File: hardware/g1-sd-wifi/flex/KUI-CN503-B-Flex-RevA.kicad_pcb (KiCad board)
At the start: 2 copper layers, 10.7 x 59.9 mm, 2 parts, among them J1 CN503 row B solder contacts, J2 20-pin bottom-contact FPC tail

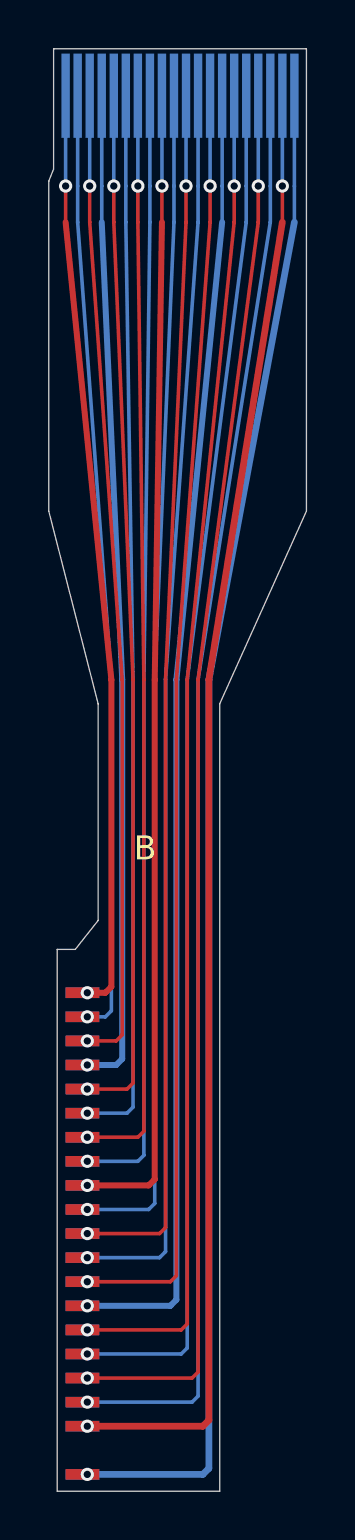
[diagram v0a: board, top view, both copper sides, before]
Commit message: G1 safety: fuse the host 3.3-V entry; no console 5 V on the flex or carrier
Host 3.3 V reached about 30 carrier parts straight from two flex contacts,
and the two console-5-V contacts were joined by an unused carrier trace;
a short on either would load a console supply through 0.5 A connector
contacts with no fuse anywhere. Now:

- F21 (0467.500NR, 0.5 A fast, same 467 family as F20) sits between the one
  remaining 3.3-V entry, J51 B1, and CONSOLE_3V3. If it opens the buffers
  lose VCCB and isolate, and U25 reports the host rail absent.
- CN503 A1 (second 3.3 V) and A3/B3 (5 V) get no flex copper at all: no
  landing pad, no trace, only an unconnected mating finger, so a chafed
  flex cannot short a console supply. Their carrier socket pins are bare.
  flex-interface.json lists them; the flex and carrier generators and both
  checks read that list. Flex ERC/DRC/parity 0; carrier ERC 0, integration
  check pass (362 parts).
- The DSN export keeps the 5-V and storage supply nets on the 1 oz outer
  layers: on 0.5 oz inner copper a 0.25 mm track at the fuse current would
  overheat (IPC-2221).
- F21 is placed by the floorplan next to J51; board DRC 0, parity 0
  (unrouted).

Co-Authored-By: Claude Opus 5.5 <noreply@anthropic.com>
Claude-Session: https://claude.ai/code/session_01Gp9EYc2r9fMpZ7V8WtfonZ
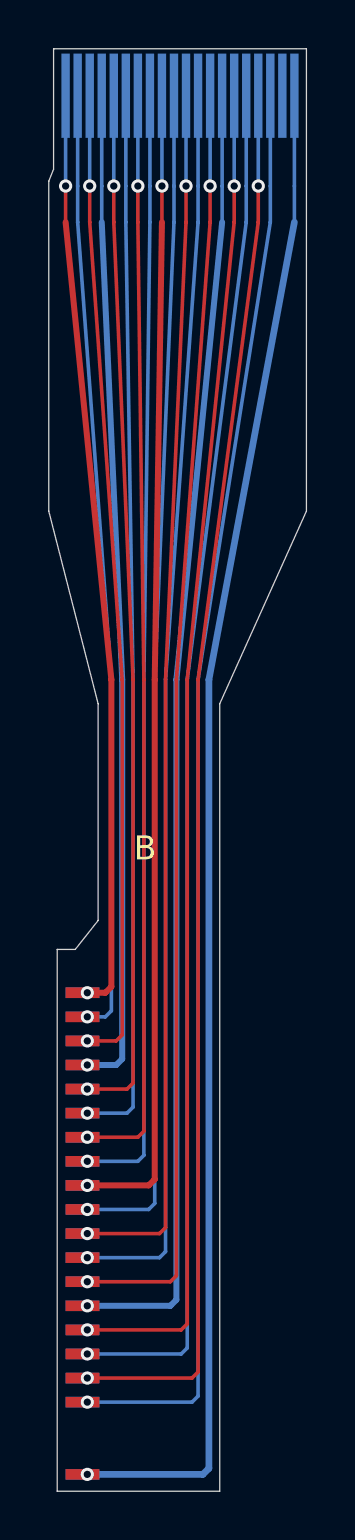
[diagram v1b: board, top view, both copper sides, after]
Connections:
- J2 pad 19: /CN503_B3_CONSOLE_5V -> unconnected-(J2-Pad19)
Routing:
- net /CN503_B3_CONSOLE_5V: track 60.8 -> 0.00 mm, vias 2 -> 0
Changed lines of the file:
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@@
 (net 0 "")
 (net 1 "/CN503_B1_CONSOLE_3V3")
-(net 2 "/CN503_B3_CONSOLE_5V")
 (net 3 "/CN503_B4_ATA_DD6")
 (net 4 "/CN503_B5_ATA_DD9")
@@
 (net 19 "/CN503_B20_ATA_CS1n")
 (net 20 "/CN503_B21_GND")
+(net 21 "unconnected-(J2-Pad19)")
 (footprint "KUI_Flex:CN503_B_20_SolderLanding_1.00mm" (layer "F.Cu") (at 100.0 100.0) (attr board_only exclude_from_pos_files exclude_from_bom)
 (property "Reference" "J1" (at 0 0) (layer "F.Fab") (effects (font (size .8 .8)) hide))
@@
 (pad "1" smd rect (at 0.7 0) (size 1.4 .44) (layers "F.Cu" "F.Mask") (net 1 "/CN503_B1_CONSOLE_3V3") (solder_mask_margin .29))
 (pad "1" smd rect (at 0.7 0) (size 1.4 .44) (layers "B.Cu" "B.Mask") (net 1 "/CN503_B1_CONSOLE_3V3") (solder_mask_margin .29))
-(pad "3" smd rect (at 0.7 -2) (size 1.4 .44) (layers "F.Cu" "F.Mask") (net 2 "/CN503_B3_CONSOLE_5V") (solder_mask_margin .29))
-(pad "3" smd rect (at 0.7 -2) (size 1.4 .44) (layers "B.Cu" "B.Mask") (net 2 "/CN503_B3_CONSOLE_5V") (solder_mask_margin .29))
 (pad "4" smd rect (at 0.7 -3) (size 1.4 .44) (layers "F.Cu" "F.Mask") (net 3 "/CN503_B4_ATA_DD6") (solder_mask_margin .29))
 (pad "4" smd rect (at 0.7 -3) (size 1.4 .44) (layers "B.Cu" "B.Mask") (net 3 "/CN503_B4_ATA_DD6") (solder_mask_margin .29))
@@
 (property "Value" "20-pin bottom-contact FPC tail" (at 0 0) (layer "F.Fab") (effects (font (size .8 .8)) hide))
 (pad "20" smd rect (at 9.5 -57.25) (size .35 3.5) (layers "B.Cu" "B.Mask") (net 1 "/CN503_B1_CONSOLE_3V3") (solder_mask_margin .10))
-(pad "19" smd rect (at 9 -57.25) (size .35 3.5) (layers "B.Cu" "B.Mask") (net 2 "/CN503_B3_CONSOLE_5V") (solder_mask_margin .10))
+(pad "19" smd rect (at 9 -57.25) (size .35 3.5) (layers "B.Cu" "B.Mask") (net 21 "unconnected-(J2-Pad19)") (solder_mask_margin .10))
 (pad "18" smd rect (at 8.5 -57.25) (size .35 3.5) (layers "B.Cu" "B.Mask") (net 3 "/CN503_B4_ATA_DD6") (solder_mask_margin .10))
 (pad "17" smd rect (at 8 -57.25) (size .35 3.5) (layers "B.Cu" "B.Mask") (net 4 "/CN503_B5_ATA_DD9") (solder_mask_margin .10))
@@
 (segment (start 109.5 48) (end 109.5 46.5) (width 0.15) (layer "B.Cu") (net 1))
 (segment (start 109.5 46.5) (end 109.5 42.75) (width 0.15) (layer "B.Cu") (net 1))
-(segment (start 100.7 98) (end 100.9 98) (width 0.15) (layer "F.Cu") (net 2))
-(segment (start 100.7 98) (end 100.9 98) (width 0.15) (layer "B.Cu") (net 2))
-(segment (start 100.9 98) (end 105.7 98) (width 0.28) (layer "F.Cu") (net 2))
-(segment (start 105.7 98) (end 105.95 97.75) (width 0.28) (layer "F.Cu") (net 2))
-(segment (start 105.95 97.75) (end 105.95 67) (width 0.28) (layer "F.Cu") (net 2))
-(segment (start 105.95 67) (end 109 48) (width 0.28) (layer "F.Cu") (net 2))
-(segment (start 109 48) (end 109 46.5) (width 0.15) (layer "F.Cu") (net 2))
-(segment (start 109 46.5) (end 109 42.75) (width 0.15) (layer "B.Cu") (net 2))
 (segment (start 100.7 97) (end 100.9 97) (width 0.15) (layer "F.Cu") (net 3))
 (segment (start 100.7 97) (end 100.9 97) (width 0.15) (layer "B.Cu") (net 3))
@@
 (segment (start 100 46.5) (end 100 42.75) (width 0.15) (layer "B.Cu") (net 20))
 (via (at 100.9 100) (size .55) (drill .3) (layers "F.Cu" "B.Cu") (net 1))
-(via (at 100.9 98) (size .55) (drill .3) (layers "F.Cu" "B.Cu") (net 2))
-(via (at 109 46.5) (size .55) (drill .3) (layers "F.Cu" "B.Cu") (net 2))
 (via (at 100.9 97) (size .55) (drill .3) (layers "F.Cu" "B.Cu") (net 3))
 (via (at 100.9 96) (size .55) (drill .3) (layers "F.Cu" "B.Cu") (net 4))
